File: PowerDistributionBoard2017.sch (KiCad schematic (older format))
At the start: 26 parts, among them J1 Main Computer (Jetson), J10 Drive 1, J11 Drive 2, J12 Drive 3, J13 Drive 4, J14 Digger 1, J15 Digger 2, J16 Bucket 1, J17 Bucket 2, J18 MAux 1, J19 Conn_02x02_Counter_Clockwise, J2 IMU, J3 Localization, J4 Second Computer, J5 Aux 1, J6 Aux 2, J7 Aux 3, J8 Main Button, J9 JM Button, K1 Main Relay, K2 Secondary Relay

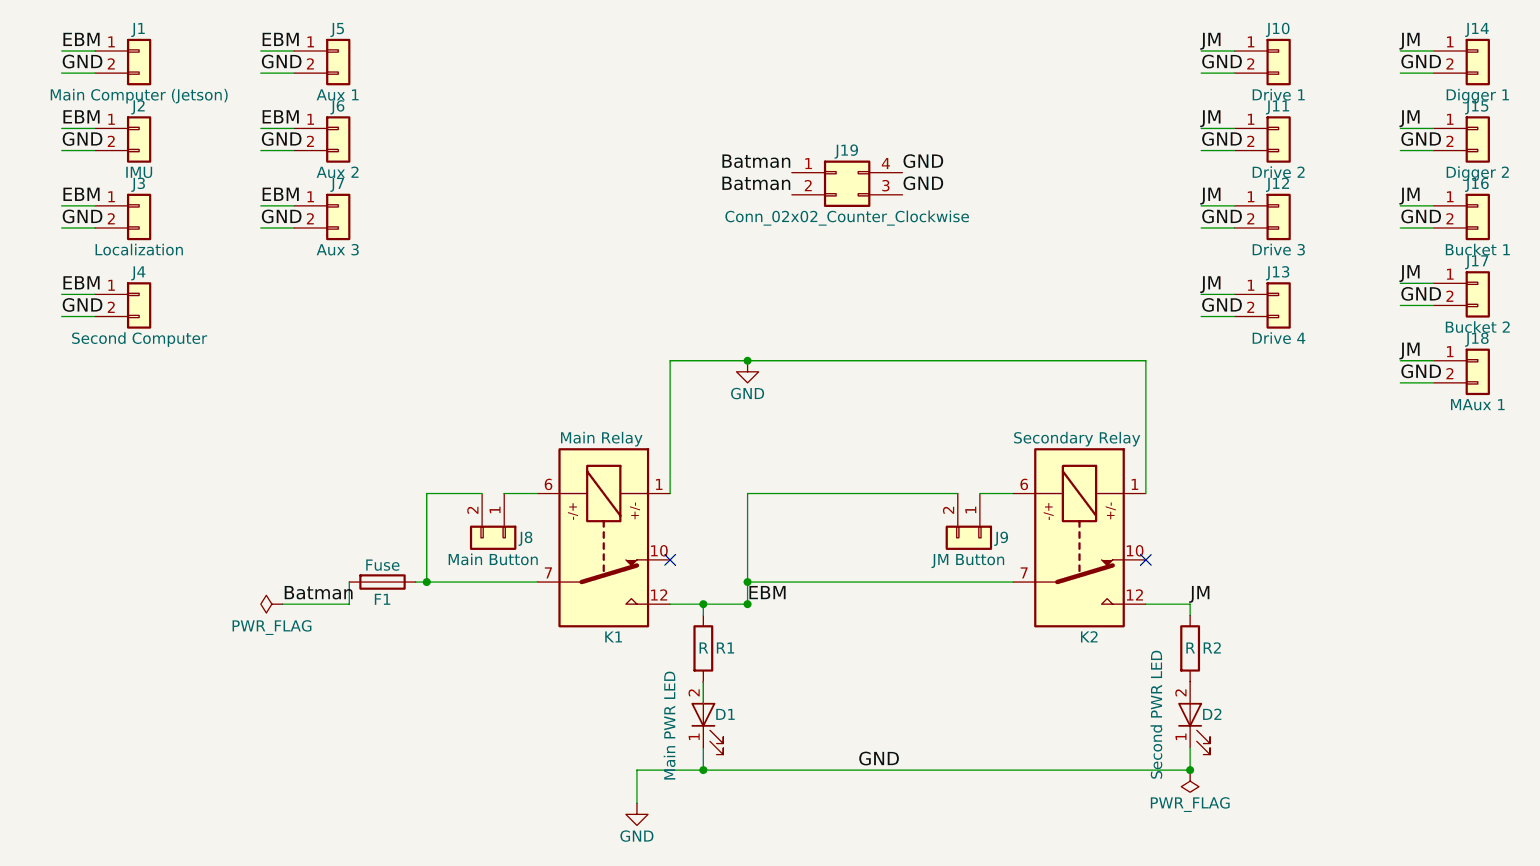
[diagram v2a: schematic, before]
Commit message: Ready for layout - Created new footprints - relay - fuse
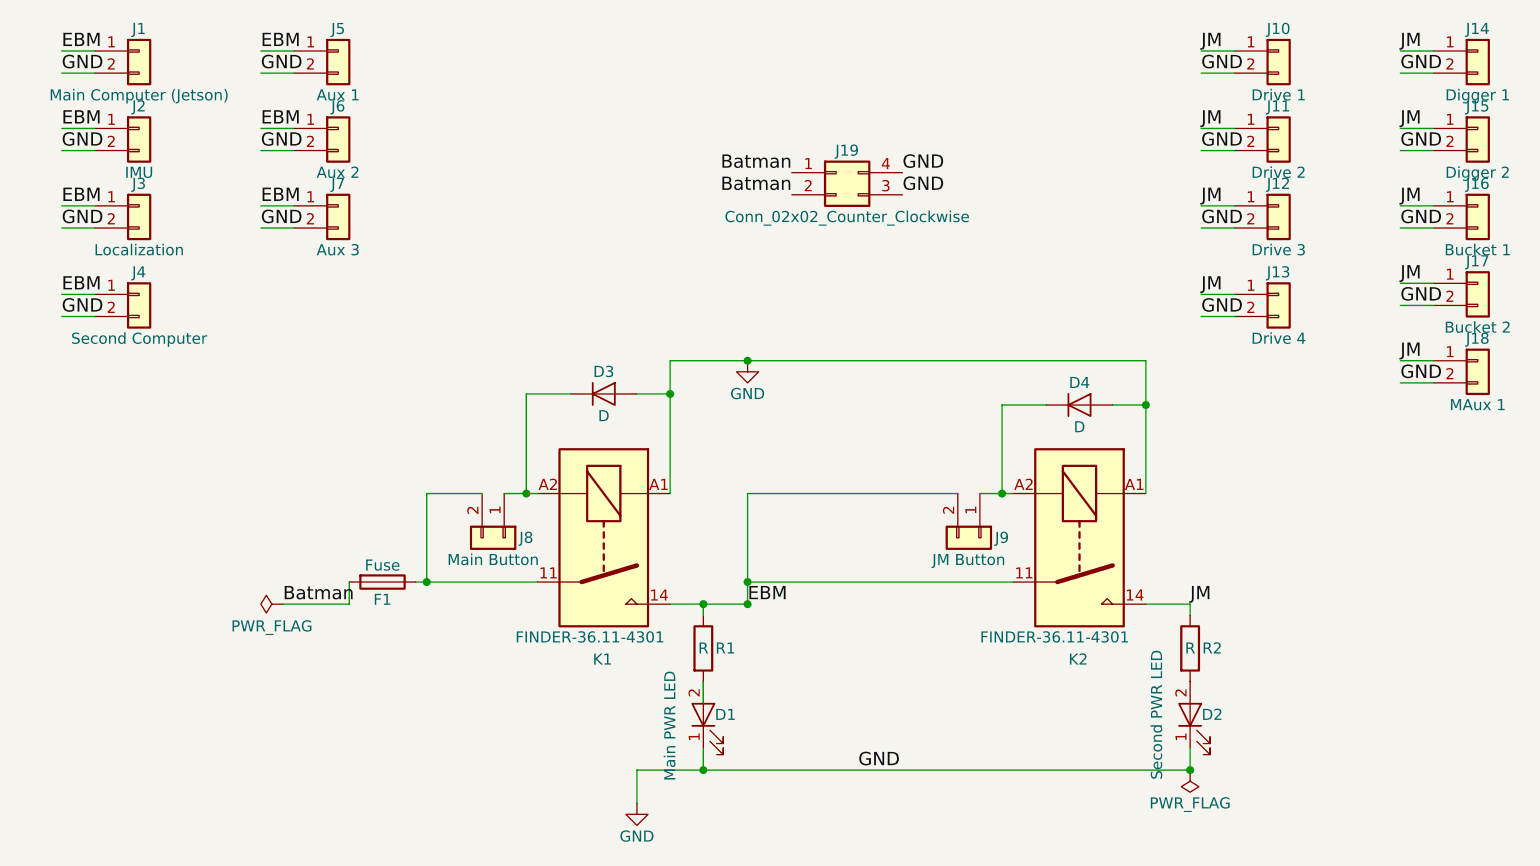
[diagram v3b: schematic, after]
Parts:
- removed K1: Main Relay, Relays_THT:Relay_SPDT_OMRON-G6E, symbol G6EU
- removed K2: Secondary Relay, Relays_THT:Relay_SPDT_OMRON-G6E, symbol G6EU
- added D3, D4: D, Diodes_SMD:D_SMA_Handsoldering, symbol D
- added K1, K2: FINDER-36.11-4301, PDB17:Relay_Through_Hole, symbol FINDER-36.11-4301
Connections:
- net EBM: now also K1.14, K2.11
- net GND: now also D3.2 (A), D4.2 (A), K1.A1, K2.A1
- net JM: now also K2.14
- net at J8.1 (Pin_1): now also D3.1 (K), K1.A2
- net at F1.1, J8.2 (Pin_2): now also K1.11
- net at J9.1 (Pin_1): now also D4.1 (K), K2.A2
- no-connect marks 2 -> 0
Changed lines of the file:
@@
-$EndComp
-$Comp
-L G6EU K1
-U 1 1 59F39B7C
-P 4850 3150
-F 0 "K1" V 5300 3150 50  0000 L CNN
-F 1 "Main Relay" V 4400 2950 50  0000 L CNN
-F 2 "Relays_THT:Relay_SPDT_OMRON-G6E" H 5980 3120 50  0001 C CNN
-F 3 "" H 4850 3150 50  0001 C CNN
-	1    4850 3150
-	0    1    1    0
-$EndComp
-$Comp
-L G6EU K2
-U 1 1 59F39D37
-P 7000 3150
-F 0 "K2" V 7450 3150 50  0000 L CNN
-F 1 "Secondary Relay" V 6550 2850 50  0000 L CNN
-F 2 "Relays_THT:Relay_SPDT_OMRON-G6E" H 8130 3120 50  0001 C CNN
-F 3 "" H 7000 3150 50  0001 C CNN
-	1    7000 3150
-	0    1    1    0
 $EndComp
 $Comp
@@
 Text Label 8450 2450 0    60   ~ 0
 GND
-NoConn ~ 5150 3250
-NoConn ~ 7300 3250
 $Comp
 L Conn_02x02_Counter_Clockwise J19
@@
 	-1   0    0    1
 $EndComp
+$Comp
+L FINDER-36.11-4301 K1
+U 1 1 5A04EBD0
+P 4850 3150
+F 0 "K1" V 5400 3100 50  0000 L CNN
+F 1 "FINDER-36.11-4301" V 5300 2750 50  0000 L CNN
+F 2 "PDB17:Relay_Through_Hole" H 6120 3120 50  0001 C CNN
+F 3 "" H 4850 3150 50  0001 C CNN
+	1    4850 3150
+	0    1    1    0
+$EndComp
+$Comp
+L FINDER-36.11-4301 K2
+U 1 1 5A05401A
+P 7000 3150
+F 0 "K2" V 7550 3100 50  0000 L CNN
+F 1 "FINDER-36.11-4301" V 7450 2700 50  0000 L CNN
+F 2 "PDB17:Relay_Through_Hole" H 8270 3120 50  0001 C CNN
+F 3 "" H 7000 3150 50  0001 C CNN
+	1    7000 3150
+	0    1    1    0
+$EndComp
+$Comp
+L D D3
+U 1 1 5A054570
+P 4850 2500
+F 0 "D3" H 4850 2600 50  0000 C CNN
+F 1 "D" H 4850 2400 50  0000 C CNN
+F 2 "Diodes_SMD:D_SMA_Handsoldering" H 4850 2500 50  0001 C CNN
+F 3 "" H 4850 2500 50  0001 C CNN
+	1    4850 2500
+	1    0    0    -1
+$EndComp
+$Comp
+L D D4
+U 1 1 5A0545D7
+P 7000 2550
+F 0 "D4" H 7000 2650 50  0000 C CNN
+F 1 "D" H 7000 2450 50  0000 C CNN
+F 2 "Diodes_SMD:D_SMA_Handsoldering" H 7000 2550 50  0001 C CNN
+F 3 "" H 7000 2550 50  0001 C CNN
+	1    7000 2550
+	1    0    0    -1
+$EndComp
+Wire Wire Line
+	6650 2950 6650 2550
+Wire Wire Line
+	6650 2550 6850 2550
+Connection ~ 6650 2950
+Wire Wire Line
+	7150 2550 7300 2550
+Connection ~ 7300 2550
+Wire Wire Line
+	5000 2500 5150 2500
+Connection ~ 5150 2500
+Wire Wire Line
+	4700 2500 4500 2500
+Wire Wire Line
+	4500 2500 4500 2950
+Connection ~ 4500 2950
 $EndSCHEMATC

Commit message: Made layout
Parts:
- F1: footprint Connectors_Molex:Molex_MegaFit_2x01x5.70mm_Angled -> PDB17:ATC_Fuse_Holder
- R1, R2: value R -> 750
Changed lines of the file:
@@
 F 0 "F1" V 3930 3350 50  0000 C CNN
 F 1 "Fuse" V 3775 3350 50  0000 C CNN
-F 2 "Connectors_Molex:Molex_MegaFit_2x01x5.70mm_Angled" V 3780 3350 50  0001 C CNN
+F 2 "PDB17:ATC_Fuse_Holder" V 3780 3350 50  0001 C CNN
 F 3 "" H 3850 3350 50  0001 C CNN
 	1    3850 3350
@@
 P 5300 3650
 F 0 "R1" H 5400 3650 50  0000 C CNN
-F 1 "R" H 5300 3650 50  0000 C CNN
+F 1 "750" H 5300 3650 50  0000 C CNN
 F 2 "Resistors_SMD:R_1206_HandSoldering" V 5230 3650 50  0001 C CNN
 F 3 "" H 5300 3650 50  0001 C CNN
@@
 P 7500 3650
 F 0 "R2" H 7600 3650 50  0000 C CNN
-F 1 "R" H 7500 3650 50  0000 C CNN
+F 1 "750" H 7500 3650 50  0000 C CNN
 F 2 "Resistors_SMD:R_1206_HandSoldering" V 7430 3650 50  0001 C CNN
 F 3 "" H 7500 3650 50  0001 C CNN
